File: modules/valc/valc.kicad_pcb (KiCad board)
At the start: 2 copper layers, 40.6 x 40.6 mm, 42 parts, among them J1 2, J10 11, J11 12, J12 13, J13 A0, J14 A1, J15 A2, J16 A3, J17 A4, J18 A5, J19 Vcc, J2 3, J20 Gnd, J3 4, J4 5, J5 6, J6 7, J7 8, J8 9, J9 10, SW1001 Rotary_Encoder_Switch, U1 74LS139

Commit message: Fix 74LS139 pins
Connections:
- U1 pad 2: Net-(J12-Pad1) -> Net-(J11-Pad1)
- U1 pad 3: Net-(J11-Pad1) -> Net-(J12-Pad1)
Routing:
- net (no net): track 0.00 -> 3.49 mm
- net Net-(J12-Pad1): track 27.2 -> 30.2 mm
- net Net-(J11-Pad1): track 47.9 -> 49.5 mm
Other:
- board text added: "07.11.2020"
- board text added: "hash"
- board text added: "v2.1"

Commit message: Fix hash, add gerber
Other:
- rule solder_mask_min_width: 0.25 -> 0.1
- board text added: "f9b630"
- board text removed: "hash"
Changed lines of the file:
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@@
     (pad_drill 1)
     (pad_to_mask_clearance 0.051)
-    (solder_mask_min_width 0.25)
+    (solder_mask_min_width 0.1)
     (aux_axis_origin 0 0)
     (visible_elements 7FFFFFFF)
     (pcbplotparams
-      (layerselection 0x00000_fffffffe)
+      (layerselection 0x010f0_ffffffff)
       (usegerberextensions false)
       (usegerberattributes false)
@@
       (hpglpenspeed 20)
       (hpglpendiameter 15.000000)
-      (psnegative true)
+      (psnegative false)
       (psa4output false)
       (plotreference true)
@@
       (padsonsilk false)
       (subtractmaskfromsilk false)
-      (outputformat 4)
+      (outputformat 1)
       (mirror false)
-      (drillshape 1)
+      (drillshape 0)
       (scaleselection 1)
-      (outputdirectory ""))
+      (outputdirectory "gerber/"))
   )
   (net 0 "")
@@
       (effects (font (size 0.5 0.5) (thickness 0.08)) (justify mirror))
     )
-    (pad 1 smd roundrect (at -1.025 0 90) (size 1.15 1.4) (layers B.Cu B.Paste B.Mask) (roundrect_rratio 0.217391)
+    (pad 1 smd roundrect (at -1.025 0 90) (size 1.15 1.4) (layers B.Cu B.Paste B.Mask) (roundrect_rratio 0.2173904347826087)
       (net 23 VCC))
-    (pad 2 smd roundrect (at 1.025 0 90) (size 1.15 1.4) (layers B.Cu B.Paste B.Mask) (roundrect_rratio 0.217391)
+    (pad 2 smd roundrect (at 1.025 0 90) (size 1.15 1.4) (layers B.Cu B.Paste B.Mask) (roundrect_rratio 0.2173904347826087)
       (net 17 "Net-(D1001-Pad2)"))
     (model ${KISYS3DMOD}/Resistor_SMD.3dshapes/R_0805_2012Metric.wrl
@@
       (effects (font (size 0.5 0.5) (thickness 0.08)) (justify mirror))
     )
-    (pad 2 smd roundrect (at 1.025 0 270) (size 1.15 1.4) (layers B.Cu B.Paste B.Mask) (roundrect_rratio 0.217391)
+    (pad 2 smd roundrect (at 1.025 0 270) (size 1.15 1.4) (layers B.Cu B.Paste B.Mask) (roundrect_rratio 0.2173904347826087)
       (net 20 GND))
-    (pad 1 smd roundrect (at -1.025 0 270) (size 1.15 1.4) (layers B.Cu B.Paste B.Mask) (roundrect_rratio 0.217391)
+    (pad 1 smd roundrect (at -1.025 0 270) (size 1.15 1.4) (layers B.Cu B.Paste B.Mask) (roundrect_rratio 0.2173904347826087)
       (net 21 "Net-(C1-Pad1)"))
     (model ${KISYS3DMOD}/Capacitor_SMD.3dshapes/C_0805_2012Metric.wrl
@@
       (effects (font (size 0.5 0.5) (thickness 0.08)) (justify mirror))
     )
-    (pad 1 smd roundrect (at -1.025 0 270) (size 1.15 1.4) (layers B.Cu B.Paste B.Mask) (roundrect_rratio 0.217391)
+    (pad 1 smd roundrect (at -1.025 0 270) (size 1.15 1.4) (layers B.Cu B.Paste B.Mask) (roundrect_rratio 0.2173904347826087)
       (net 22 "Net-(C2-Pad1)"))
-    (pad 2 smd roundrect (at 1.025 0 270) (size 1.15 1.4) (layers B.Cu B.Paste B.Mask) (roundrect_rratio 0.217391)
+    (pad 2 smd roundrect (at 1.025 0 270) (size 1.15 1.4) (layers B.Cu B.Paste B.Mask) (roundrect_rratio 0.2173904347826087)
       (net 20 GND))
     (model ${KISYS3DMOD}/Capacitor_SMD.3dshapes/C_0805_2012Metric.wrl
@@
       (effects (font (size 0.5 0.5) (thickness 0.08)) (justify mirror))
     )
-    (pad 1 smd roundrect (at -1.025 0 270) (size 1.15 1.4) (layers B.Cu B.Paste B.Mask) (roundrect_rratio 0.217391)
+    (pad 1 smd roundrect (at -1.025 0 270) (size 1.15 1.4) (layers B.Cu B.Paste B.Mask) (roundrect_rratio 0.2173904347826087)
       (net 23 VCC))
-    (pad 2 smd roundrect (at 1.025 0 270) (size 1.15 1.4) (layers B.Cu B.Paste B.Mask) (roundrect_rratio 0.217391)
+    (pad 2 smd roundrect (at 1.025 0 270) (size 1.15 1.4) (layers B.Cu B.Paste B.Mask) (roundrect_rratio 0.2173904347826087)
       (net 20 GND))
     (model ${KISYS3DMOD}/Capacitor_SMD.3dshapes/C_0805_2012Metric.wrl
@@
       (effects (font (size 0.5 0.5) (thickness 0.08)) (justify mirror))
     )
-    (pad 1 smd roundrect (at -1.025 0 270) (size 1.15 1.4) (layers B.Cu B.Paste B.Mask) (roundrect_rratio 0.217391)
+    (pad 1 smd roundrect (at -1.025 0 270) (size 1.15 1.4) (layers B.Cu B.Paste B.Mask) (roundrect_rratio 0.2173904347826087)
       (net 23 VCC))
-    (pad 2 smd roundrect (at 1.025 0 270) (size 1.15 1.4) (layers B.Cu B.Paste B.Mask) (roundrect_rratio 0.217391)
+    (pad 2 smd roundrect (at 1.025 0 270) (size 1.15 1.4) (layers B.Cu B.Paste B.Mask) (roundrect_rratio 0.2173904347826087)
       (net 29 "Net-(R1-Pad2)"))
     (model ${KISYS3DMOD}/Resistor_SMD.3dshapes/R_0805_2012Metric.wrl
@@
       (effects (font (size 0.5 0.5) (thickness 0.08)) (justify mirror))
     )
-    (pad 2 smd roundrect (at 1.025 0 90) (size 1.15 1.4) (layers B.Cu B.Paste B.Mask) (roundrect_rratio 0.217391)
+    (pad 2 smd roundrect (at 1.025 0 90) (size 1.15 1.4) (layers B.Cu B.Paste B.Mask) (roundrect_rratio 0.2173904347826087)
       (net 21 "Net-(C1-Pad1)"))
-    (pad 1 smd roundrect (at -1.025 0 90) (size 1.15 1.4) (layers B.Cu B.Paste B.Mask) (roundrect_rratio 0.217391)
+    (pad 1 smd roundrect (at -1.025 0 90) (size 1.15 1.4) (layers B.Cu B.Paste B.Mask) (roundrect_rratio 0.2173904347826087)
       (net 29 "Net-(R1-Pad2)"))
     (model ${KISYS3DMOD}/Resistor_SMD.3dshapes/R_0805_2012Metric.wrl
@@
       (effects (font (size 0.5 0.5) (thickness 0.08)) (justify mirror))
     )
-    (pad 1 smd roundrect (at -1.025 0 270) (size 1.15 1.4) (layers B.Cu B.Paste B.Mask) (roundrect_rratio 0.217391)
+    (pad 1 smd roundrect (at -1.025 0 270) (size 1.15 1.4) (layers B.Cu B.Paste B.Mask) (roundrect_rratio 0.2173904347826087)
       (net 23 VCC))
-    (pad 2 smd roundrect (at 1.025 0 270) (size 1.15 1.4) (layers B.Cu B.Paste B.Mask) (roundrect_rratio 0.217391)
+    (pad 2 smd roundrect (at 1.025 0 270) (size 1.15 1.4) (layers B.Cu B.Paste B.Mask) (roundrect_rratio 0.2173904347826087)
       (net 30 "Net-(R3-Pad2)"))
     (model ${KISYS3DMOD}/Resistor_SMD.3dshapes/R_0805_2012Metric.wrl
@@
       (effects (font (size 0.5 0.5) (thickness 0.08)) (justify mirror))
     )
-    (pad 2 smd roundrect (at 1.025 0 90) (size 1.15 1.4) (layers B.Cu B.Paste B.Mask) (roundrect_rratio 0.217391)
+    (pad 2 smd roundrect (at 1.025 0 90) (size 1.15 1.4) (layers B.Cu B.Paste B.Mask) (roundrect_rratio 0.2173904347826087)
       (net 22 "Net-(C2-Pad1)"))
-    (pad 1 smd roundrect (at -1.025 0 90) (size 1.15 1.4) (layers B.Cu B.Paste B.Mask) (roundrect_rratio 0.217391)
+    (pad 1 smd roundrect (at -1.025 0 90) (size 1.15 1.4) (layers B.Cu B.Paste B.Mask) (roundrect_rratio 0.2173904347826087)
       (net 30 "Net-(R3-Pad2)"))
     (model ${KISYS3DMOD}/Resistor_SMD.3dshapes/R_0805_2012Metric.wrl
@@
       (effects (font (size 0.5 0.5) (thickness 0.08)) (justify mirror))
     )
-    (pad 1 smd roundrect (at -1.025 0 90) (size 1.15 1.4) (layers B.Cu B.Paste B.Mask) (roundrect_rratio 0.217391)
+    (pad 1 smd roundrect (at -1.025 0 90) (size 1.15 1.4) (layers B.Cu B.Paste B.Mask) (roundrect_rratio 0.2173904347826087)
       (net 23 VCC))
-    (pad 2 smd roundrect (at 1.025 0 90) (size 1.15 1.4) (layers B.Cu B.Paste B.Mask) (roundrect_rratio 0.217391)
+    (pad 2 smd roundrect (at 1.025 0 90) (size 1.15 1.4) (layers B.Cu B.Paste B.Mask) (roundrect_rratio 0.2173904347826087)
       (net 31 "Net-(R6-Pad2)"))
     (model ${KISYS3DMOD}/Resistor_SMD.3dshapes/R_0805_2012Metric.wrl
@@
     (effects (font (size 1 1) (thickness 0.2)))
   )
-  (gr_text hash (at 110.49 75.2475) (layer F.Cu)
+  (gr_text f9b630 (at 110.49 75.2475) (layer F.Cu)
     (effects (font (size 1 1) (thickness 0.2)))
   )

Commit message: Valcoder polishing
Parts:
- renumbered D1004 to D2, D1001 to D3, D1002 to D4, SW1001 to SW1, D1 to VD1, D2 to VD2, D3 to VD3, D4 to VD4
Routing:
- net Net-(D2-Pad2): track 47.0 -> 66.5 mm
- net Net-(D4-Pad1): track 5.63 -> 12.1 mm
- net Net-(D3-Pad1): track 23.1 -> 29.6 mm
- net Net-(D2-Pad1): track 9.35 -> 15.9 mm

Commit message: Fix hash, fix gerber
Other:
- board text added: "031ab0"
- board text added: "11.11.2020"
- board text removed: "07.11.2020"
- board text removed: "f9b630"

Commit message: Valc. Add silk.
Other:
- board text added: "05.12.2020"
- board text added: "74HC139"
- board text removed: "11.11.2020"

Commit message: Fix hash, add gerber
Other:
- board text added: "9fe84b"
- board text removed: "031ab0"

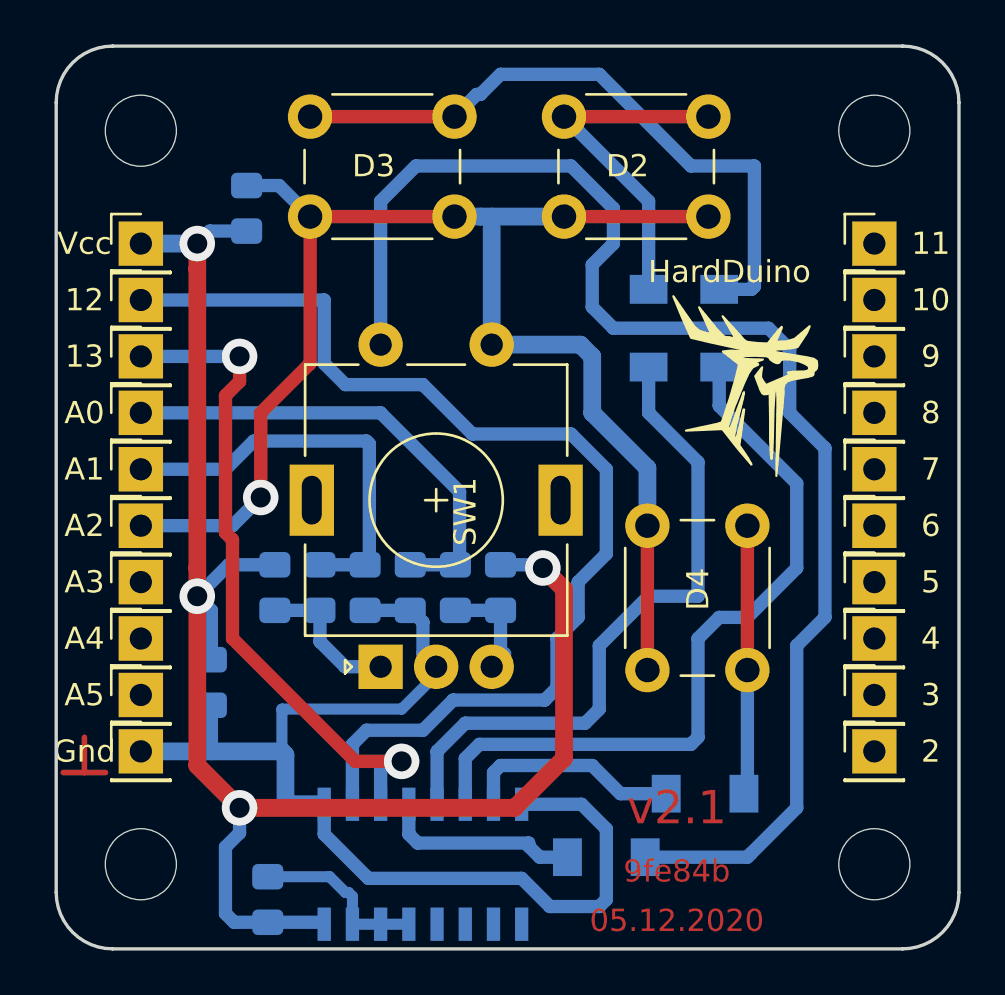
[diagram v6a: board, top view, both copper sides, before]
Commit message: 1x PCBs. Move holes to edges. Caution! This changes is uncompatible with previous versions...
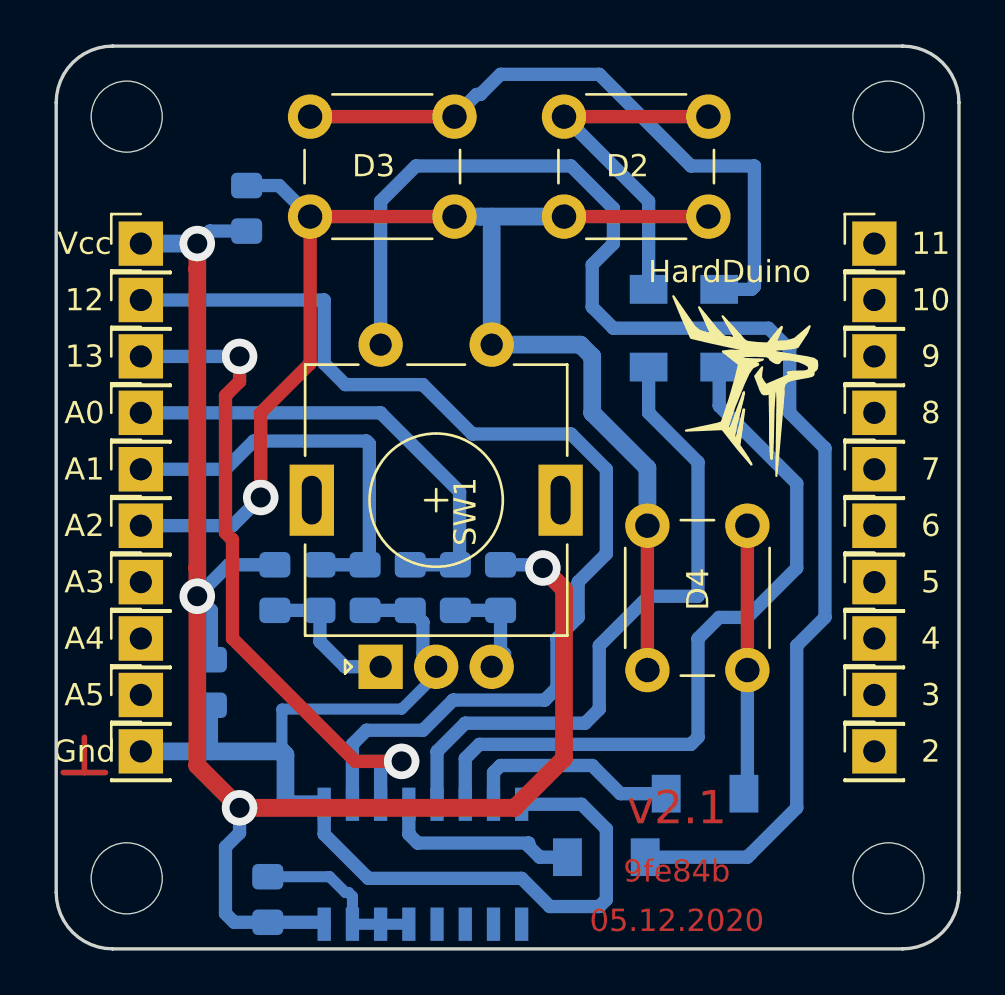
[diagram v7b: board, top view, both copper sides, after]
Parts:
- moved H1 0.90 mm to (85.7, 41.3)
- moved H3 0.90 mm to (120.0, 41.3)
- moved H2 0.90 mm to (85.7, 75.6)
- moved H4 0.90 mm to (120.0, 75.6)
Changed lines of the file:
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@@
   )
   (module MountingHole:MountingHole_3.2mm_M3 (layer F.Cu)
-    (at 86.36 41.91)
+    (at 85.7250 41.2750)
     (descr "Mounting Hole 3.2mm, no annular, M3")
     (tags "mounting hole 3.2mm no annular m3")
@@
   )
   (module MountingHole:MountingHole_3.2mm_M3 (layer F.Cu)
-    (at 86.36 74.93)
+    (at 85.7250 75.5650)
     (descr "Mounting Hole 3.2mm, no annular, M3")
     (tags "mounting hole 3.2mm no annular m3")
@@
   )
   (module MountingHole:MountingHole_3.2mm_M3 (layer F.Cu)
-    (at 119.38 41.91)
+    (at 120.0150 41.2750)
     (descr "Mounting Hole 3.2mm, no annular, M3")
     (tags "mounting hole 3.2mm no annular m3")
@@
   )
   (module MountingHole:MountingHole_3.2mm_M3 (layer F.Cu)
-    (at 119.38 74.93)
+    (at 120.0150 75.5650)
     (descr "Mounting Hole 3.2mm, no annular, M3")
     (tags "mounting hole 3.2mm no annular m3")

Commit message: Fix hash & version
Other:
- board text added: "21.02.2021"
- board text added: "b4d799"
- board text added: "v2.3"
- board text removed: "05.12.2020"
- board text removed: "9fe84b"
- board text removed: "v2.1"
